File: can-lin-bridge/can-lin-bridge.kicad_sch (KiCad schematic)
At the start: 11 parts, among them IC1 PIC18F26Q83T-I_5N, J1 ICSP, U1 TJA1029TK/20/1J, U2 TJA1042TK/3/2Z

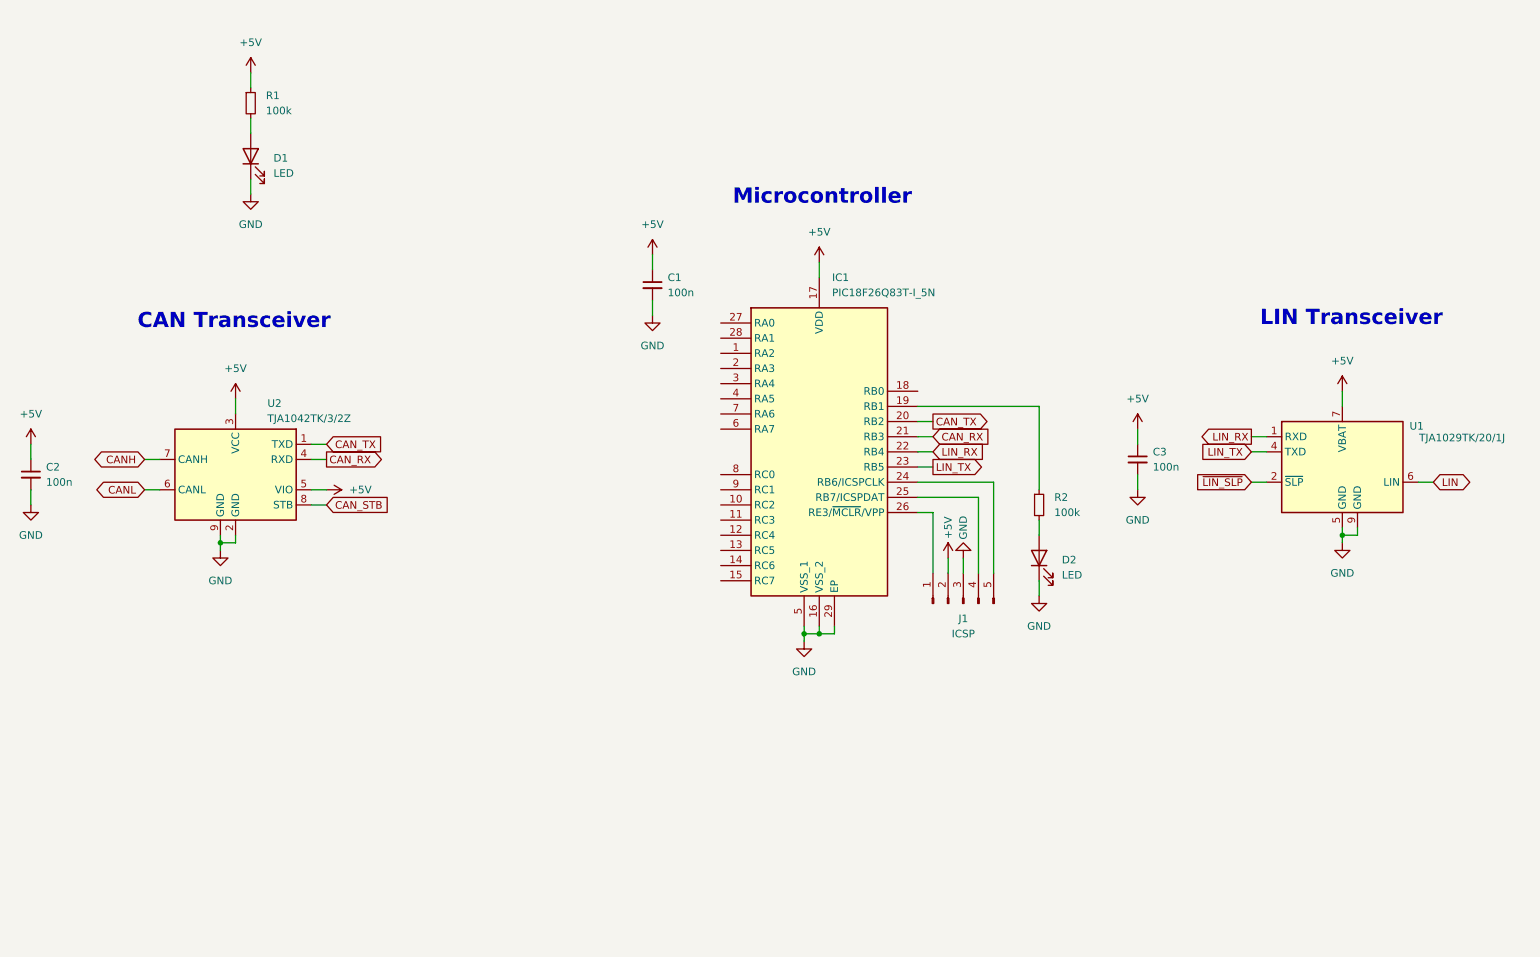
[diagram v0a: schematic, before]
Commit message: can-lin-bridge: Add mounting holes & test point
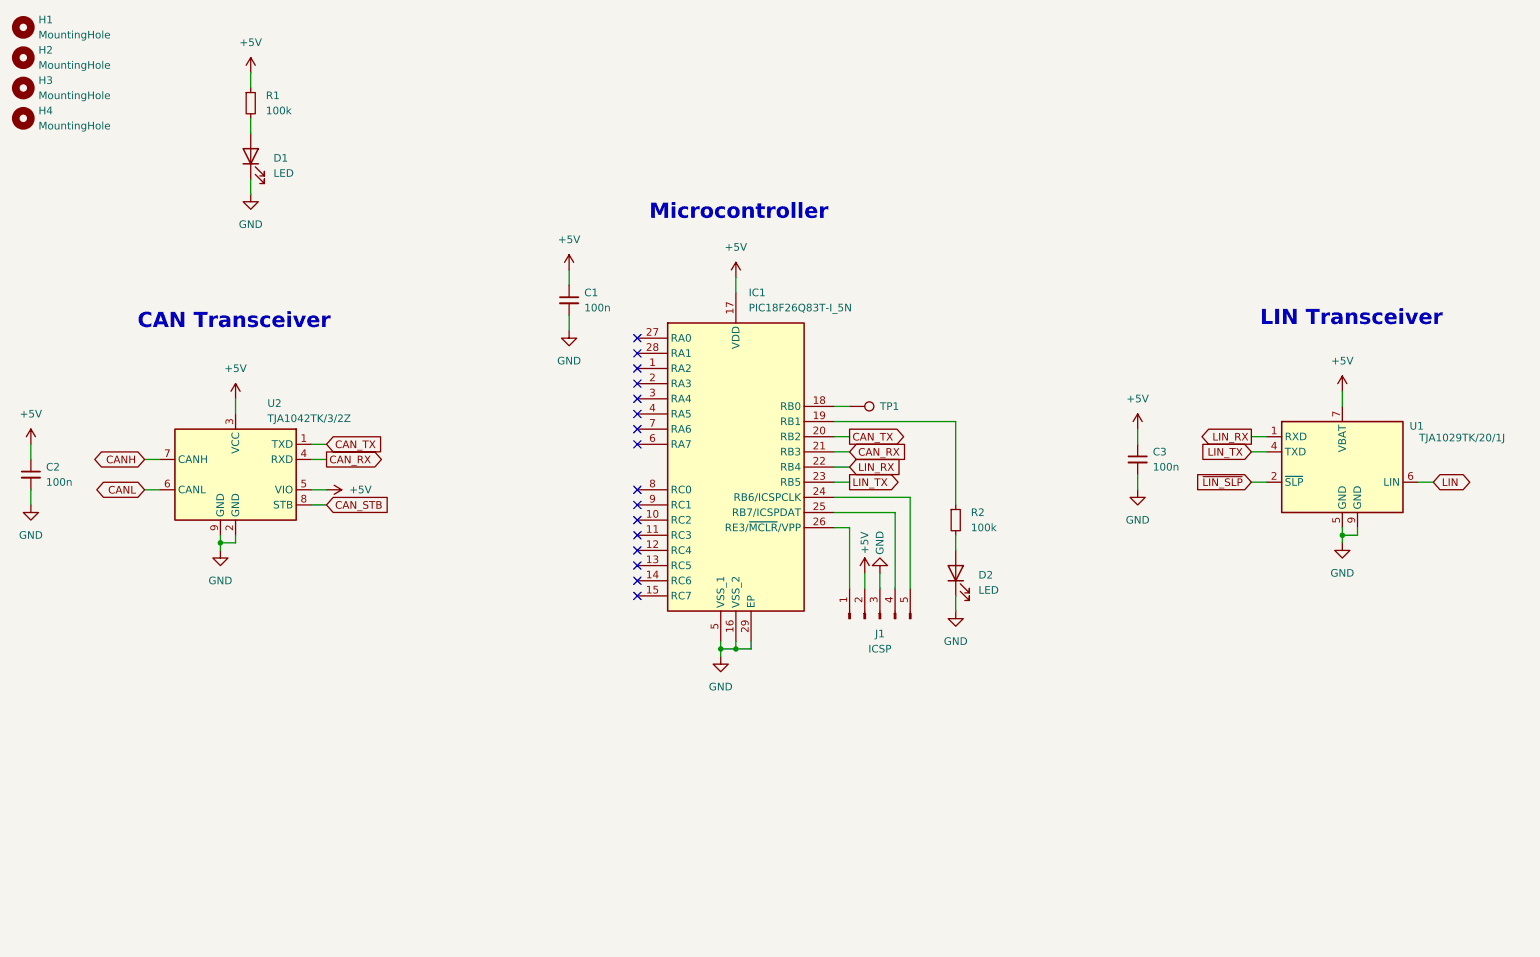
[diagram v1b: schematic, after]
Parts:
- added H1, H2, H3, H4: MountingHole, symbol Mechanical:MountingHole
- added TP1: TestPoint, symbol Connector:TestPoint
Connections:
- net at IC1.18 (RB0): now also TP1.1
- no-connect marks 0 -> 16
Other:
- moved on the sheet: C1, D2, IC1, J1, R2

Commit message: can-lin-bridge: Add footprints to all components
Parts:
- C1, C2, C3: footprint (none) -> Capacitor_SMD:C_0402_1005Metric
- D1, D2: footprint (none) -> LED_SMD:LED_0402_1005Metric
- H1, H2, H3, H4: footprint (none) -> MountingHole:MountingHole_2.2mm_M2
- IC1: footprint QFN65P600X600X100-29N-D -> PIC18F26Q83T-I5N:QFN65P600X600X100-29N-D
- J1: footprint (none) -> Connector_PinHeader_1.27mm:PinHeader_1x05_P1.27mm_Vertical
- R1, R2: footprint (none) -> Resistor_SMD:R_0402_1005Metric
- TP1: footprint (none) -> TestPoint:TestPoint_Pad_D1.0mm
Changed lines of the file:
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@@
 			)
 		)
-		(property "Footprint" "QFN65P600X600X100-29N-D"
+		(property "Footprint" "PIC18F26Q83T-I5N:QFN65P600X600X100-29N-D"
 			(at 153.67 168.58 0)
 			(effects
@@
 			)
 		)
-		(property "Footprint" ""
+		(property "Footprint" "MountingHole:MountingHole_2.2mm_M2"
 			(at 21.59 26.67 0)
 			(effects
@@
 			)
 		)
-		(property "Footprint" ""
+		(property "Footprint" "Capacitor_SMD:C_0402_1005Metric"
 			(at 22.86 96.52 0)
 			(effects
@@
 			)
 		)
-		(property "Footprint" ""
+		(property "Footprint" "Resistor_SMD:R_0402_1005Metric"
 			(at 59.69 34.29 0)
 			(effects
@@
 			)
 		)
-		(property "Footprint" ""
+		(property "Footprint" "LED_SMD:LED_0402_1005Metric"
 			(at 177.8 113.03 0)
 			(effects
@@
 			)
 		)
-		(property "Footprint" ""
+		(property "Footprint" "Capacitor_SMD:C_0402_1005Metric"
 			(at 113.03 67.31 0)
 			(effects
@@
 			)
 		)
-		(property "Footprint" ""
+		(property "Footprint" "LED_SMD:LED_0402_1005Metric"
 			(at 59.69 43.18 0)
 			(effects
@@
 			)
 		)
-		(property "Footprint" ""
+		(property "Footprint" "TestPoint:TestPoint_Pad_D1.0mm"
 			(at 160.02 90.17 0)
 			(effects
@@
 			)
 		)
-		(property "Footprint" ""
+		(property "Footprint" "MountingHole:MountingHole_2.2mm_M2"
 			(at 21.59 31.75 0)
 			(effects
@@
 			)
 		)
-		(property "Footprint" ""
+		(property "Footprint" "Capacitor_SMD:C_0402_1005Metric"
 			(at 208.28 93.98 0)
 			(effects
@@
 			)
 		)
-		(property "Footprint" ""
+		(property "Footprint" "Connector_PinHeader_1.27mm:PinHeader_1x05_P1.27mm_Vertical"
 			(at 165.1 120.65 0)
 			(effects
@@
 			)
 		)
-		(property "Footprint" ""
+		(property "Footprint" "MountingHole:MountingHole_2.2mm_M2"
 			(at 21.59 21.59 0)
 			(effects
@@
 			)
 		)
-		(property "Footprint" ""
+		(property "Footprint" "MountingHole:MountingHole_2.2mm_M2"
 			(at 21.59 36.83 0)
 			(effects
@@
 			)
 		)
-		(property "Footprint" ""
+		(property "Footprint" "Resistor_SMD:R_0402_1005Metric"
 			(at 177.8 104.14 0)
 			(effects

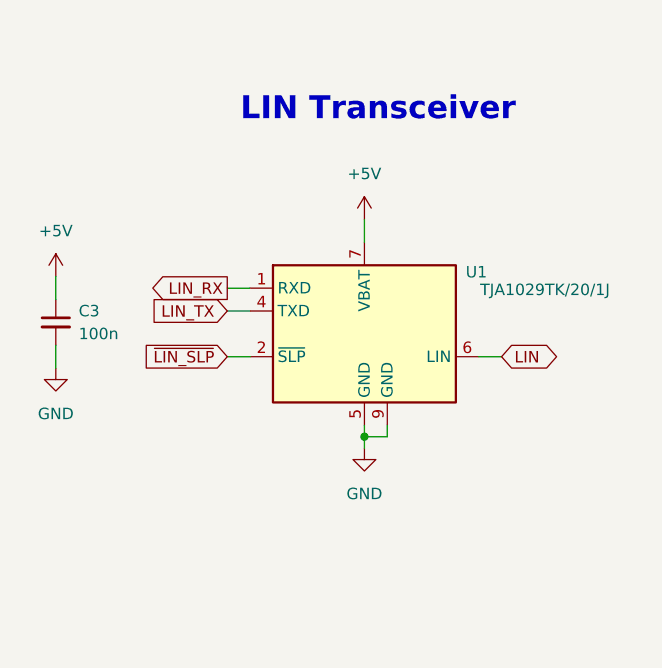
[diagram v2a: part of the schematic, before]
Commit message: can-lin-bridge: Add in auxiliary components for LIN bus
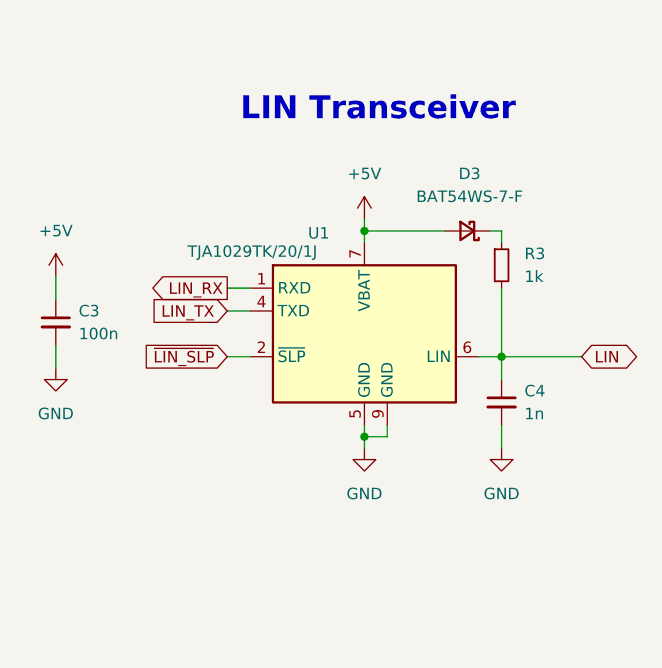
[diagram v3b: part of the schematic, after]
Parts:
- added C4: 1n, Capacitor_SMD:C_0402_1005Metric, symbol Device:C_Small
- added D3: BAT54WS-7-F, Diode_SMD:D_SOD-323, symbol Device:D_Schottky_Small
- added R3: 1k, Resistor_SMD:R_0402_1005Metric, symbol Device:R_Small
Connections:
- net +5V: now also D3.2 (A)
- net GND: now also C4.2
- net LIN: now also C4.1, R3.2
- new net: D3.1 (K), R3.1

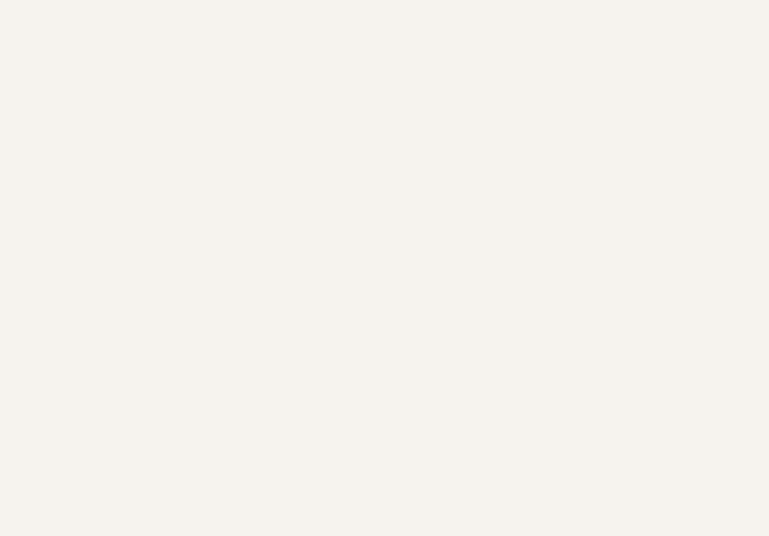
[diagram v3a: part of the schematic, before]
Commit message: can-lin-bridge: Add CAN bus, LIN bus, and power connectors to schematic
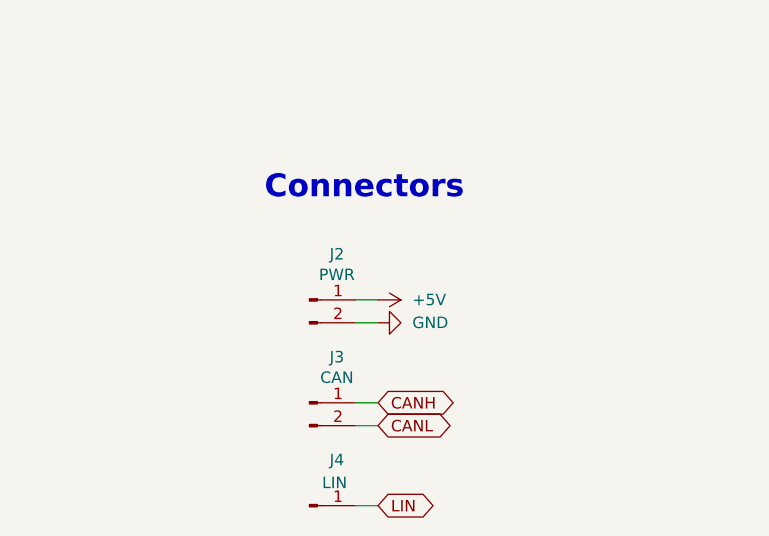
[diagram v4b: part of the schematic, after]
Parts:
- added J2: PWR, Connector_PinHeader_2.54mm:PinHeader_1x02_P2.54mm_Vertical, symbol Connector:Conn_01x02_Pin
- added J3: CAN, Connector_PinHeader_2.54mm:PinHeader_1x02_P2.54mm_Vertical, symbol Connector:Conn_01x02_Pin
- added J4: LIN, Connector_PinHeader_2.54mm:PinHeader_1x01_P2.54mm_Vertical, symbol Connector:Conn_01x01_Pin
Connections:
- net +5V: now also J2.1 (Pin_1)
- net CANH: now also J3.1 (Pin_1)
- net CANL: now also J3.2 (Pin_2)
- net GND: now also J2.2 (Pin_2)
- net LIN: now also J4.1 (Pin_1)
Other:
- note added: "Connectors"
